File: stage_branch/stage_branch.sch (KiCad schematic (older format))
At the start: 1 part, among them P1 DIN_41612_128P

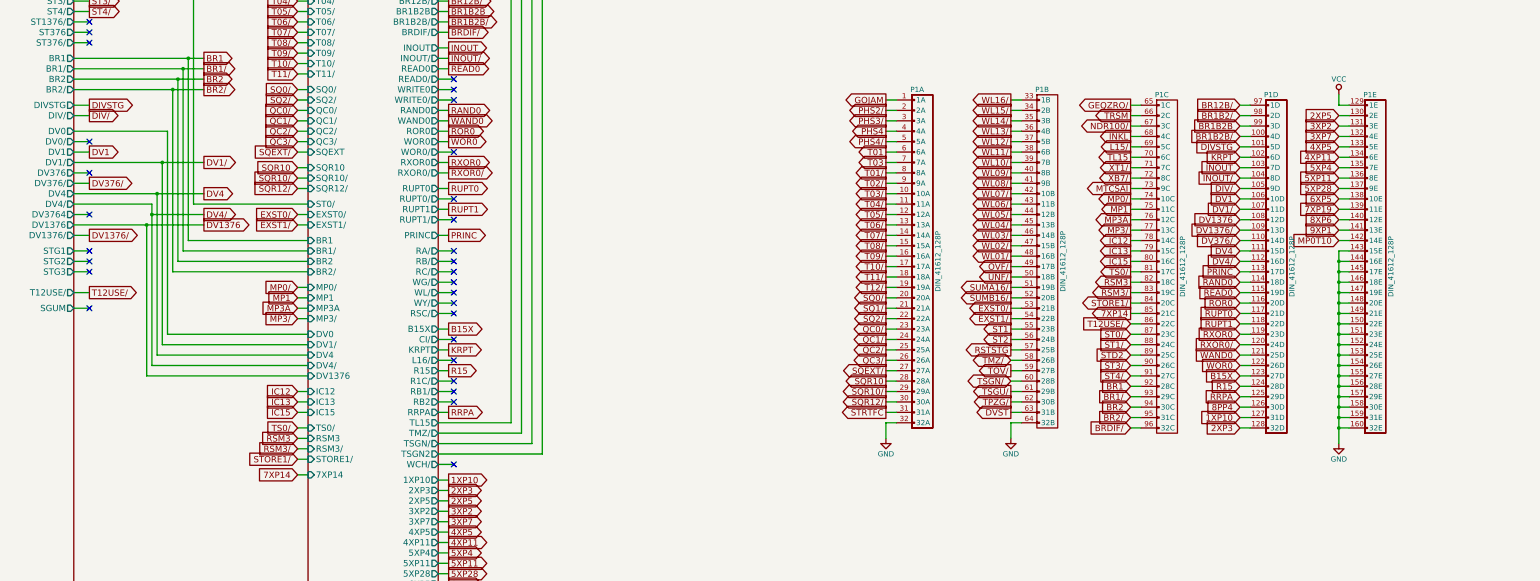
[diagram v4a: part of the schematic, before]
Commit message: Tied in module 7, and corrected lots of errors.
Off the top of my head:
* T12DC/ not actually connected to restart logic in A02-2
* IC12/ and IC13 schematic errors
* Lots of gates moved from later modules up to modules 2-7
* YT0..7 logic dropped from 7, it belongs in 14
* Lots of missing signal breakouts
* ...probably some other things, I should keep a list as I go

All control pulses associated with GOJ1 now behave correctly during
GOJ1.
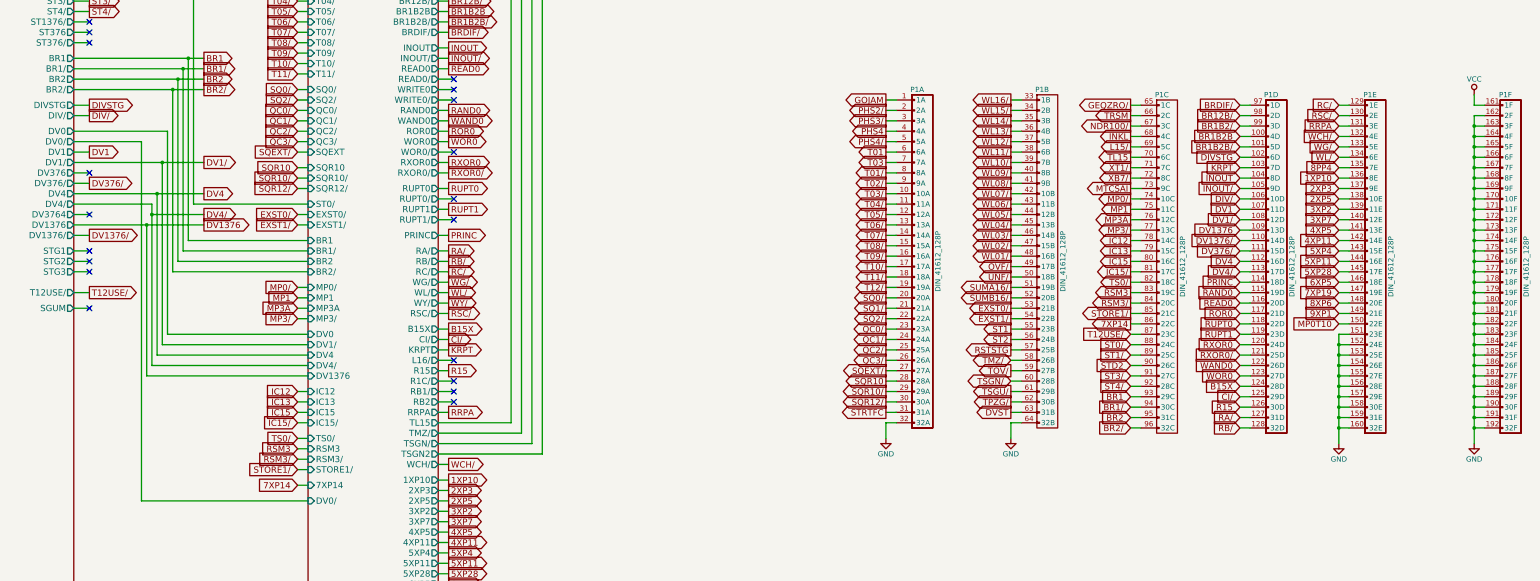
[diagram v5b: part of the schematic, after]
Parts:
- added unit 6 of P1
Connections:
- net 1XP10: now also P1.136 (8E); no longer P1.127 (31D)
- net 2XP3: now also P1.137 (9E); no longer P1.128 (32D)
- net 2XP5: now also P1.138 (10E); no longer P1.130 (2E)
- net 3XP2: now also P1.139 (11E); no longer P1.131 (3E)
- net 3XP7: now also P1.140 (12E); no longer P1.132 (4E)
- net 4XP11: now also P1.142 (14E); no longer P1.134 (6E)
- net 4XP5: now also P1.141 (13E); no longer P1.133 (5E)
- net 5XP11: now also P1.144 (16E); no longer P1.136 (8E)
- net 5XP28: now also P1.145 (17E); no longer P1.137 (9E)
- net 5XP4: now also P1.143 (15E); no longer P1.135 (7E)
- net 6XP5: now also P1.146 (18E); no longer P1.138 (10E)
- net 7XP14: now also P1.86 (22C); no longer P1.85 (21C)
- net 7XP19: now also P1.147 (19E); no longer P1.139 (11E)
- net 8PP4: now also P1.135 (7E); no longer P1.126 (30D)
- net 8XP6: now also P1.148 (20E); no longer P1.140 (12E)
- net 9XP1: now also P1.149 (21E); no longer P1.141 (13E)
- net B15X: now also P1.124 (28D); no longer P1.123 (27D)
- net BR1: now also P1.93 (29C); no longer P1.92 (28C)
- net BR1/: now also P1.94 (30C); no longer P1.93 (29C)
- net BR12B/: now also P1.98 (2D); no longer P1.97 (1D)
- net BR1B2/: now also P1.99 (3D); no longer P1.98 (2D)
- net BR1B2B: now also P1.100 (4D); no longer P1.99 (3D)
- net BR1B2B/: now also P1.101 (5D); no longer P1.100 (4D)
- net BR2: now also P1.95 (31C); no longer P1.94 (30C)
- net BR2/: now also P1.96 (32C); no longer P1.95 (31C)
- net BRDIF/: now also P1.97 (1D); no longer P1.96 (32C)
- net DIV/: now also P1.106 (10D); no longer P1.105 (9D)
- net DIVSTG: now also P1.102 (6D); no longer P1.101 (5D)
- net DV1: now also P1.107 (11D); no longer P1.106 (10D)
- net DV1/: now also P1.108 (12D); no longer P1.107 (11D)
- net DV1376: now also P1.109 (13D); no longer P1.108 (12D)
- net DV1376/: now also P1.110 (14D); no longer P1.109 (13D)
- net DV376/: now also P1.111 (15D); no longer P1.110 (14D)
- net DV4: now also P1.112 (16D); no longer P1.111 (15D)
- net DV4/: now also P1.113 (17D); no longer P1.112 (16D)
- net GND: now also P1.162 (2F), P1.163 (3F), P1.164 (4F), P1.165 (5F), P1.166 (6F), P1.167 (7F), P1.168 (8F), P1.169 (9F), P1.170 (10F), P1.171 (11F), P1.172 (12F), P1.173 (13F), P1.174 (14F), P1.175 (15F), P1.176 (16F), P1.177 (17F), P1.178 (18F), P1.179 (19F), P1.180 (20F), P1.181 (21F), P1.182 (22F), P1.183 (23F), P1.184 (24F), P1.185 (25F), P1.186 (26F), P1.187 (27F), P1.188 (28F), P1.189 (29F), P1.190 (30F), P1.191 (31F), P1.192 (32F); no longer P1.143 (15E), P1.144 (16E), P1.145 (17E), P1.146 (18E), P1.147 (19E), P1.148 (20E), P1.149 (21E), P1.150 (22E)
- net INOUT: now also P1.104 (8D); no longer P1.103 (7D)
- net INOUT/: now also P1.105 (9D); no longer P1.104 (8D)
- net KRPT: now also P1.103 (7D); no longer P1.102 (6D)
- net MP0T10: now also P1.150 (22E); no longer P1.142 (14E)
- net PRINC: now also P1.114 (18D); no longer P1.113 (17D)
- net R15: now also P1.126 (30D); no longer P1.124 (28D)
- net RAND0: now also P1.115 (19D); no longer P1.114 (18D)
- net READ0: now also P1.116 (20D); no longer P1.115 (19D)
- net ROR0: now also P1.117 (21D); no longer P1.116 (20D)
- net RRPA: now also P1.131 (3E); no longer P1.125 (29D)
- net RSM3: now also P1.83 (19C); no longer P1.82 (18C)
- net RSM3/: now also P1.84 (20C); no longer P1.83 (19C)
- net RUPT0: now also P1.118 (22D); no longer P1.117 (21D)
- net RUPT1: now also P1.119 (23D); no longer P1.118 (22D)
- net RXOR0: now also P1.120 (24D); no longer P1.119 (23D)
- net RXOR0/: now also P1.121 (25D); no longer P1.120 (24D)
- net ST0/: now also P1.88 (24C); no longer P1.87 (23C)
- net ST1/: now also P1.89 (25C); no longer P1.88 (24C)
- net ST3/: now also P1.91 (27C); no longer P1.90 (26C)
- net ST4/: now also P1.92 (28C); no longer P1.91 (27C)
- net STD2: now also P1.90 (26C); no longer P1.89 (25C)
- net STORE1/: now also P1.85 (21C); no longer P1.84 (20C)
- net T12USE/: now also P1.87 (23C); no longer P1.86 (22C)
- net TS0/: now also P1.82 (18C); no longer P1.81 (17C)
- net VCC: now also P1.161 (1F); no longer P1.129 (1E)
- net WAND0: now also P1.122 (26D); no longer P1.121 (25D)
- net WOR0: now also P1.123 (27D); no longer P1.122 (26D)
- new net CI/: P1.125 (29D)
- new net IC15/: P1.81 (17C)
- new net RA/: P1.127 (31D)
- new net RB/: P1.128 (32D)
- new net RC/: P1.129 (1E)
- new net RSC/: P1.130 (2E)
- new net WCH/: P1.132 (4E)
- new net WG/: P1.133 (5E)
- new net WL/: P1.134 (6E)
- no-connect marks 38 -> 28

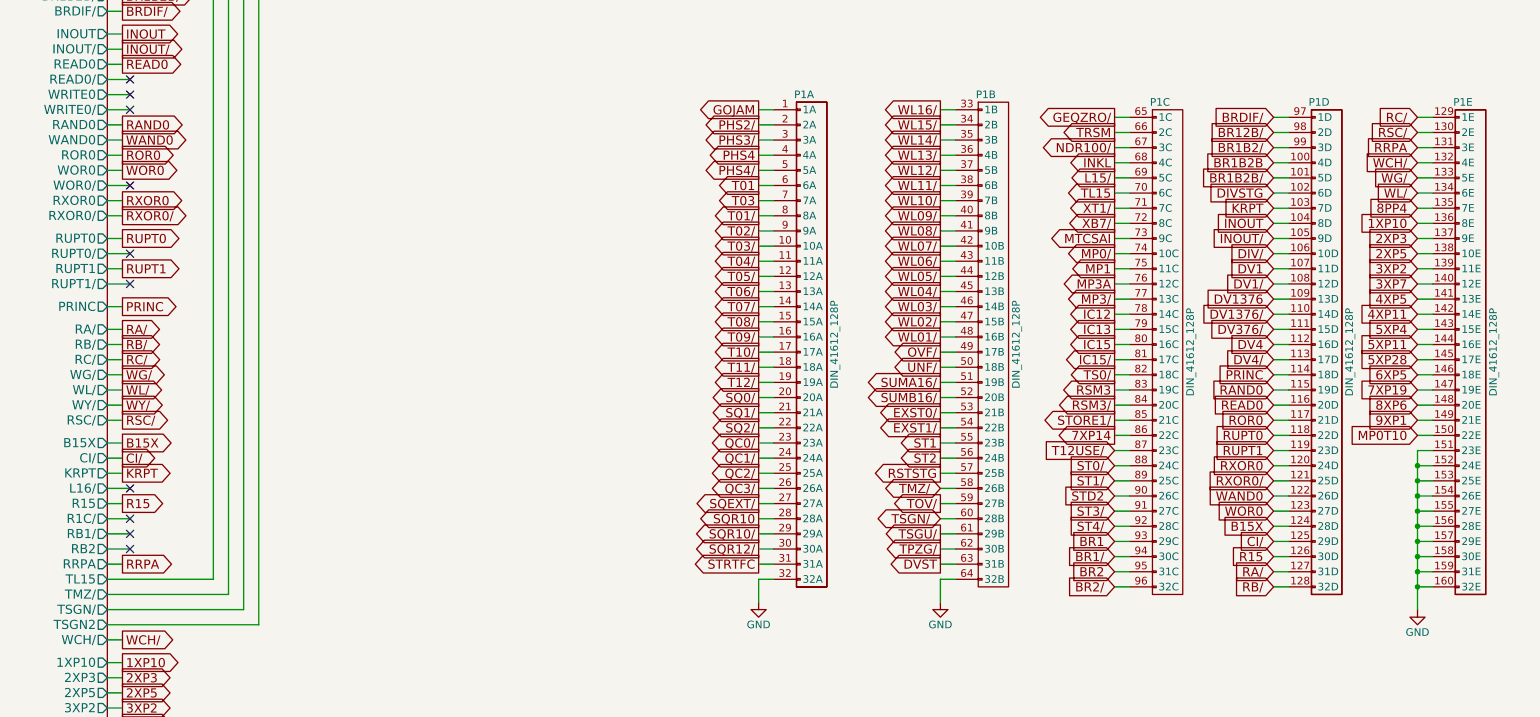
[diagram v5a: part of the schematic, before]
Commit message: Tied in module 8, and corrected lots of initial conditions.
The registers and ALU appear to work now, with TC0 and STD2 shuffling things around correctly, and Z counting up as instructions execute.
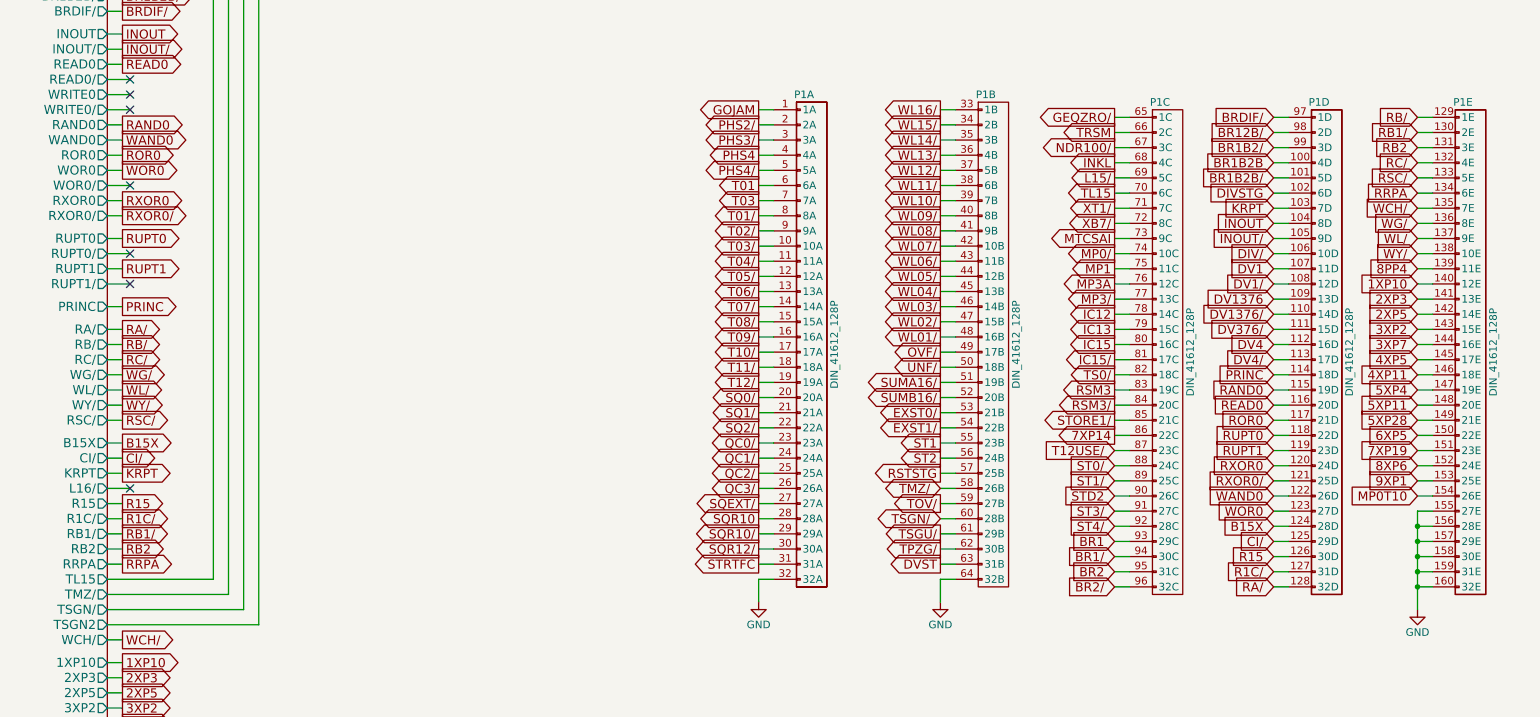
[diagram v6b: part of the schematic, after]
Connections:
- net 1XP10: now also P1.140 (12E); no longer P1.136 (8E)
- net 2XP3: now also P1.141 (13E); no longer P1.137 (9E)
- net 2XP5: now also P1.142 (14E); no longer P1.138 (10E)
- net 3XP2: now also P1.143 (15E); no longer P1.139 (11E)
- net 3XP7: now also P1.144 (16E); no longer P1.140 (12E)
- net 4XP11: now also P1.146 (18E); no longer P1.142 (14E)
- net 4XP5: now also P1.145 (17E); no longer P1.141 (13E)
- net 5XP11: now also P1.148 (20E); no longer P1.144 (16E)
- net 5XP28: now also P1.149 (21E); no longer P1.145 (17E)
- net 5XP4: now also P1.147 (19E); no longer P1.143 (15E)
- net 6XP5: now also P1.150 (22E); no longer P1.146 (18E)
- net 7XP19: now also P1.151 (23E); no longer P1.147 (19E)
- net 8PP4: now also P1.139 (11E); no longer P1.135 (7E)
- net 8XP6: now also P1.152 (24E); no longer P1.148 (20E)
- net 9XP1: now also P1.153 (25E); no longer P1.149 (21E)
- net GND: no longer P1.151 (23E), P1.152 (24E), P1.153 (25E), P1.154 (26E)
- net MP0T10: now also P1.154 (26E); no longer P1.150 (22E)
- net RA/: now also P1.128 (32D); no longer P1.127 (31D)
- net RB/: now also P1.129 (1E); no longer P1.128 (32D)
- net RC/: now also P1.132 (4E); no longer P1.129 (1E)
- net RRPA: now also P1.134 (6E); no longer P1.131 (3E)
- net RSC/: now also P1.133 (5E); no longer P1.130 (2E)
- net WCH/: now also P1.135 (7E); no longer P1.132 (4E)
- net WG/: now also P1.136 (8E); no longer P1.133 (5E)
- net WL/: now also P1.137 (9E); no longer P1.134 (6E)
- net WY/: now also P1.138 (10E)
- new net R1C/: P1.127 (31D)
- new net RB1/: P1.130 (2E)
- new net RB2: P1.131 (3E)
- no-connect marks 28 -> 25
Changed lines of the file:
@@
 Text GLabel 15900 3550 0    60   Input ~ 0
 BR1B2B
-NoConn ~ 8350 5900
-NoConn ~ 8350 6000
-NoConn ~ 8350 6100
 Text GLabel 8300 5600 2    60   Output ~ 0
 KRPT
@@
 	8300 5800 8200 5800
 Wire Wire Line
-	8350 5900 8200 5900
-Wire Wire Line
-	8350 6000 8200 6000
-Wire Wire Line
-	8200 6100 8350 6100
+	8300 5900 8200 5900
+Wire Wire Line
+	8300 6000 8200 6000
+Wire Wire Line
+	8200 6100 8300 6100
 Wire Wire Line
 	8300 6200 8200 6200
@@
 Wire Wire Line
 	8300 7550 8200 7550
-Text GLabel 16850 4650 0    60   Input ~ 0
+Text GLabel 16850 5050 0    60   Input ~ 0
 5XP4
 Wire Wire Line
-	16850 4650 16950 4650
+	16850 5050 16950 5050
 Connection ~ 5800 2800
 Text GLabel 5950 2800 2    60   Output ~ 0
@@
 Connection ~ 16850 6150
 Wire Wire Line
-	16850 5450 16950 5450
-Wire Wire Line
-	16850 5550 16950 5550
-Connection ~ 16850 5550
-Wire Wire Line
-	16850 5650 16950 5650
-Connection ~ 16850 5650
-Wire Wire Line
-	16850 5750 16950 5750
-Connection ~ 16850 5750
-Wire Wire Line
 	16850 5850 16950 5850
-Connection ~ 16850 5850
 Wire Wire Line
 	16850 5950 16950 5950
@@
 Text GLabel 8300 7650 2    60   Output ~ 0
 5XP11
-Text GLabel 16850 4750 0    60   Input ~ 0
+Text GLabel 16850 5150 0    60   Input ~ 0
 5XP11
 Wire Wire Line
-	16850 4750 16950 4750
+	16850 5150 16950 5150
 Text GLabel 8300 5400 2    60   Output ~ 0
 B15X
@@
 Text GLabel 8300 8500 2    60   Output ~ 0
 MP0T10
-Text GLabel 16850 5350 0    60   Input ~ 0
+Text GLabel 16850 5750 0    60   Input ~ 0
 MP0T10
 Wire Wire Line
-	16850 5350 16950 5350
+	16850 5750 16950 5750
 Text GLabel 8300 5800 2    60   Output ~ 0
 R15
@@
 RRPA
 Wire Wire Line
-	16850 3450 16950 3450
-Text GLabel 16850 3450 0    60   Input ~ 0
+	16850 3750 16950 3750
+Text GLabel 16850 3750 0    60   Input ~ 0
 RRPA
 Text GLabel 8300 4250 2    60   Output ~ 0
@@
 Text GLabel 8300 6850 2    60   Output ~ 0
 1XP10
-Text GLabel 16850 3950 0    60   Input ~ 0
+Text GLabel 16850 4350 0    60   Input ~ 0
 1XP10
 Text GLabel 8300 6950 2    60   Output ~ 0
 2XP3
-Text GLabel 16850 4050 0    60   Input ~ 0
+Text GLabel 16850 4450 0    60   Input ~ 0
 2XP3
 Text GLabel 8300 7050 2    60   Output ~ 0
 2XP5
-Text GLabel 16850 4150 0    60   Input ~ 0
+Text GLabel 16850 4550 0    60   Input ~ 0
 2XP5
 Text GLabel 8300 7150 2    60   Output ~ 0
 3XP2
-Text GLabel 16850 4250 0    60   Input ~ 0
+Text GLabel 16850 4650 0    60   Input ~ 0
 3XP2
 Text GLabel 8300 7250 2    60   Output ~ 0
 3XP7
-Text GLabel 16850 4350 0    60   Input ~ 0
+Text GLabel 16850 4750 0    60   Input ~ 0
 3XP7
 Text GLabel 8300 7450 2    60   Output ~ 0
 4XP11
-Text GLabel 16850 4550 0    60   Input ~ 0
+Text GLabel 16850 4950 0    60   Input ~ 0
 4XP11
 Text GLabel 8300 7750 2    60   Output ~ 0
 5XP28
-Text GLabel 16850 4850 0    60   Input ~ 0
+Text GLabel 16850 5250 0    60   Input ~ 0
 5XP28
 Text GLabel 8300 7850 2    60   Output ~ 0
 6XP5
-Text GLabel 16850 4950 0    60   Input ~ 0
+Text GLabel 16850 5350 0    60   Input ~ 0
 6XP5
 Text GLabel 8300 7950 2    60   Output ~ 0
@@
 Text GLabel 8300 8050 2    60   Output ~ 0
 8PP4
-Text GLabel 16850 5050 0    60   Input ~ 0
+Text GLabel 16850 5450 0    60   Input ~ 0
 7XP19
-Text GLabel 16850 3850 0    60   Input ~ 0
+Text GLabel 16850 4250 0    60   Input ~ 0
 8PP4
 Text GLabel 8300 8250 2    60   Output ~ 0
 8XP6
-Text GLabel 16850 5150 0    60   Input ~ 0
+Text GLabel 16850 5550 0    60   Input ~ 0
 8XP6
 Text GLabel 8300 8350 2    60   Output ~ 0
 9XP1
-Text GLabel 16850 5250 0    60   Input ~ 0
+Text GLabel 16850 5650 0    60   Input ~ 0
 9XP1
 Wire Wire Line
-	16850 3850 16950 3850
-Wire Wire Line
-	16850 3950 16950 3950
-Wire Wire Line
-	16950 4050 16850 4050
-Wire Wire Line
-	16850 4150 16950 4150
-Wire Wire Line
 	16850 4250 16950 4250
 Wire Wire Line
 	16850 4350 16950 4350
 Wire Wire Line
-	16950 4550 16850 4550
-Wire Wire Line
-	16850 4850 16950 4850
+	16950 4450 16850 4450
+Wire Wire Line
+	16850 4550 16950 4550
+Wire Wire Line
+	16850 4650 16950 4650
+Wire Wire Line
+	16850 4750 16950 4750
 Wire Wire Line
 	16950 4950 16850 4950
 Wire Wire Line
-	16850 5050 16950 5050
-Wire Wire Line
-	16950 5150 16850 5150
-Wire Wire Line
 	16850 5250 16950 5250
 Wire Wire Line
-	16850 5450 16850 6500
+	16950 5350 16850 5350
+Wire Wire Line
+	16850 5450 16950 5450
+Wire Wire Line
+	16950 5550 16850 5550
+Wire Wire Line
+	16850 5650 16950 5650
+Wire Wire Line
+	16850 5850 16850 6500
 Text GLabel 8300 7350 2    60   Output ~ 0
 4XP5
 Wire Wire Line
-	16950 4450 16850 4450
-Text GLabel 16850 4450 0    60   Input ~ 0
+	16950 4850 16850 4850
+Text GLabel 16850 4850 0    60   Input ~ 0
 4XP5
 Text GLabel 8300 5500 2    60   Output ~ 0
@@
 RA/
 Wire Wire Line
-	15900 6250 16000 6250
-Text GLabel 15900 6250 0    60   Input ~ 0
+	15900 6350 16000 6350
+Text GLabel 15900 6350 0    60   Input ~ 0
 RA/
 Text GLabel 8300 4750 2    60   Output ~ 0
 RB/
 Wire Wire Line
-	15900 6350 16000 6350
-Text GLabel 15900 6350 0    60   Input ~ 0
+	16850 3250 16950 3250
+Text GLabel 16850 3250 0    60   Input ~ 0
 RB/
 Text GLabel 8300 4850 2    60   Output ~ 0
 RC/
 Wire Wire Line
-	16850 3250 16950 3250
-Text GLabel 16850 3250 0    60   Input ~ 0
+	16850 3550 16950 3550
+Text GLabel 16850 3550 0    60   Input ~ 0
 RC/
 $Comp
@@
 RSC/
 Wire Wire Line
-	16850 3350 16950 3350
-Text GLabel 16850 3350 0    60   Input ~ 0
+	16850 3650 16950 3650
+Text GLabel 16850 3650 0    60   Input ~ 0
 RSC/
 Text GLabel 8300 6700 2    60   Output ~ 0
 WCH/
 Wire Wire Line
-	16850 3550 16950 3550
-Text GLabel 16850 3550 0    60   Input ~ 0
+	16850 3850 16950 3850
+Text GLabel 16850 3850 0    60   Input ~ 0
 WCH/
 Text GLabel 6850 6300 0    60   Input ~ 0
@@
 WG/
 Wire Wire Line
-	16850 3650 16950 3650
-Text GLabel 16850 3650 0    60   Input ~ 0
+	16850 3950 16950 3950
+Text GLabel 16850 3950 0    60   Input ~ 0
 WG/
 Text GLabel 8300 5050 2    60   Output ~ 0
 WL/
 Wire Wire Line
-	16850 3750 16950 3750
-Text GLabel 16850 3750 0    60   Input ~ 0
+	16850 4050 16950 4050
+Text GLabel 16850 4050 0    60   Input ~ 0
 WL/
 Text GLabel 8300 5150 2    60   Output ~ 0
@@
 Wire Wire Line
 	5350 7050 6950 7050
+Text GLabel 8300 6100 2    60   Output ~ 0
+RB2
+Wire Wire Line
+	16850 3450 16950 3450
+Text GLabel 16850 3450 0    60   Input ~ 0
+RB2
+Text GLabel 8300 5900 2    60   Output ~ 0
+R1C/
+Text GLabel 8300 6000 2    60   Output ~ 0
+RB1/
+Wire Wire Line
+	16850 3350 16950 3350
+Text GLabel 16850 3350 0    60   Input ~ 0
+RB1/
+Wire Wire Line
+	15900 6250 16000 6250
+Text GLabel 15900 6250 0    60   Input ~ 0
+R1C/
+Wire Wire Line
+	16850 4150 16950 4150
+Text GLabel 16850 4150 0    60   Input ~ 0
+WY/
 $EndSCHEMATC
